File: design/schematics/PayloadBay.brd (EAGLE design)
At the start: 101.6 x 53.3 mm, 72 parts, among them IC1 MC33269ST-5.0T3, IC2 MC33269D-5.0, IC3 ATMEGA2560-16AU, IC4 ATMEGA8U2-MU, IC5 LM358D, IC6 LP2985-33DBVR, Q1 16MHz, Q2 16MHz, T2 FDN340P, X1 DC21MMX, Y1 16MHz, Y2 16MHz

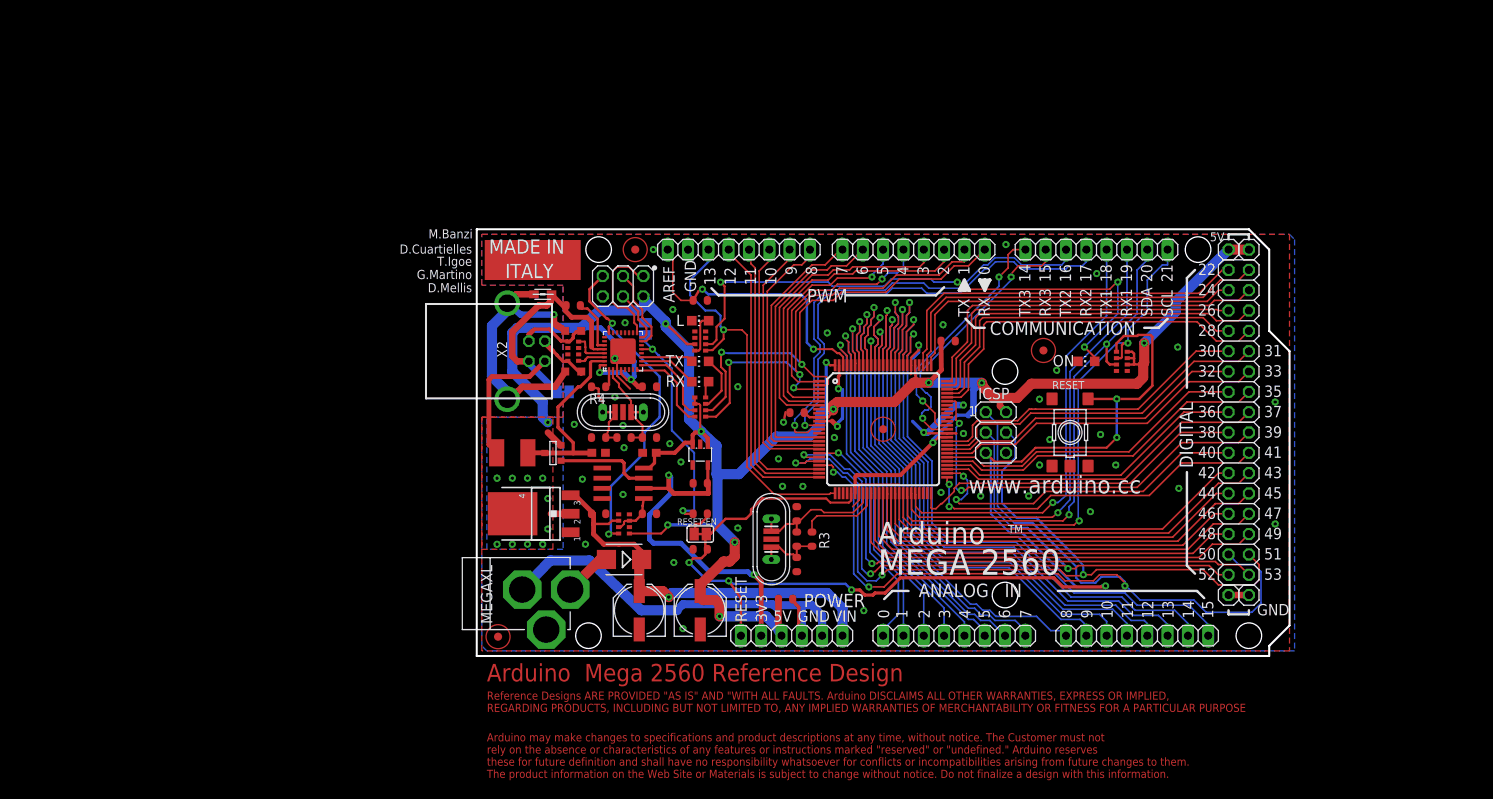
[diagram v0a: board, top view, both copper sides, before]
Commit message: updated schematics and board
* also added backup files made by eagle to gitignore
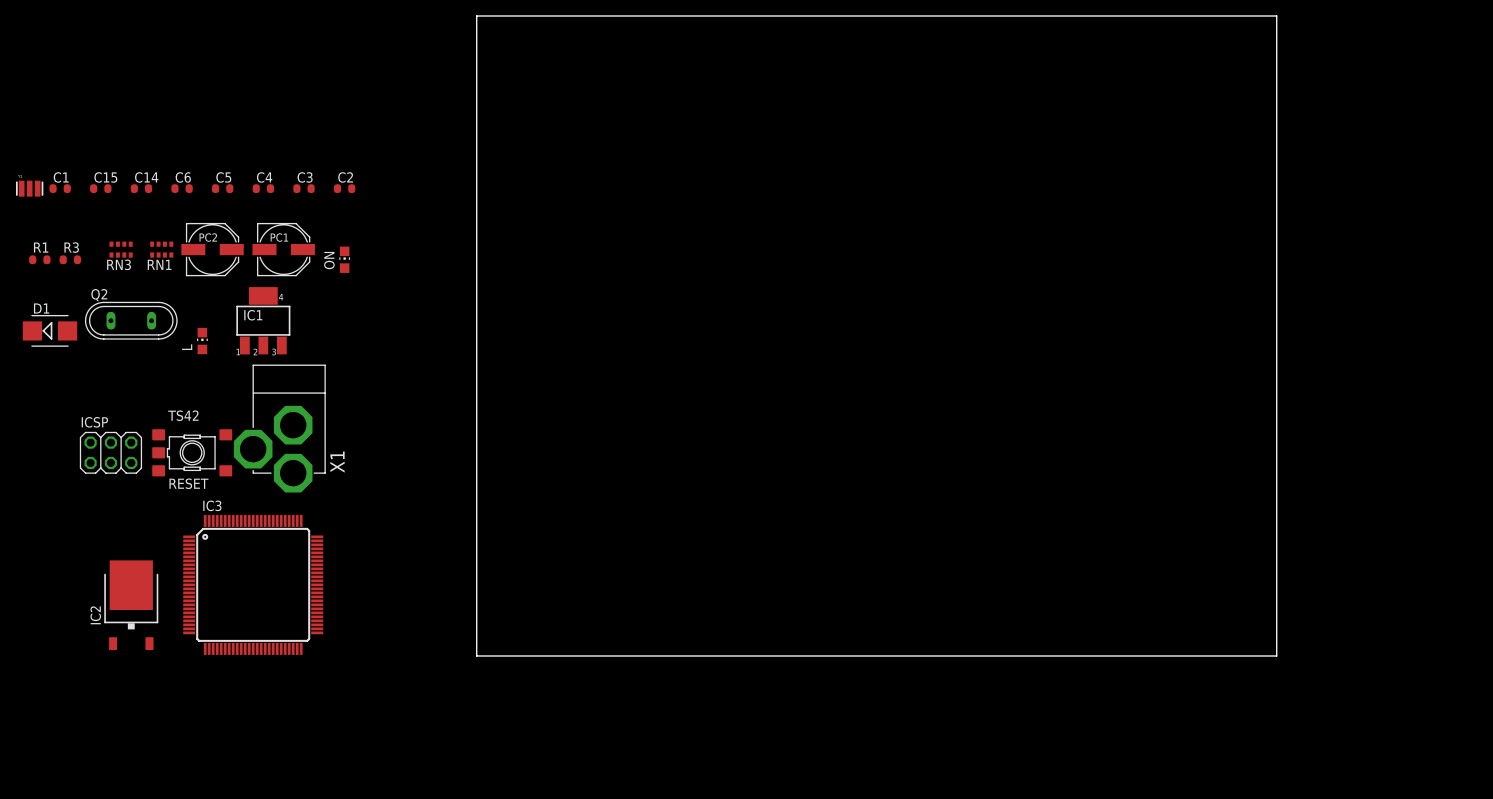
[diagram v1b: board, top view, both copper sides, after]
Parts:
- removed ADCH, ADCL, COMMUNICATION, PWMH, PWML: (no value), pinhead:1X08
- removed C10: 1u, SmartPrj:C0603-ROUND
- removed C11, C8: 100n, rcl:C0603
- removed C12, C13, C7, C9: 100n, SmartPrj:C0603-ROUND
- removed C16, C17: 22p, SmartPrj:C0603-ROUND
- removed F1: 500mA, rcl:L1812
- removed GROUND, RESET-EN, UBOOT: (no value), jumper:SJ
- removed IC4: ATMEGA8U2-MU, atmel:QFN32
- removed IC5: LM358D, linear:SO08
- removed IC6: LP2985-33DBVR, texas:SOT23-DBV
- removed ICSP1: ICSP, pinhead:2X03
- removed JP1, JP2, JP3, JP4: (no value), pinhead:1X01
- removed L1: BLM21, wuerth-elektronik:0805
- removed POWER: (no value), pinhead:1X06
- removed Q1: 16MHz, special:QS
- removed R2: 1M, SmartPrj:R0603-ROUND
- removed R4: 27R, SmartPrj:R0603-ROUND
- removed RN2: 22R, resistor-dil:CAY16
- removed RN4: 1k, resistor-dil:CAY16
- removed RN5: 10K, resistor-dil:CAT16
- removed RX, TX: YELLOW, led:CHIP-LED0805
- removed T2: FDN340P, zetex:SOT-23
- removed U$2, U$3, U$4, U$5: FIDUCIALMOUNT, SmartPrj:FIDUCIA-MOUNT
- removed X2: (no value), SmartPrj:PN61729
- removed XIOH, XIOL: (no value), pinhead:2X08
- removed Y2: 16MHz, SmartPrj:RESONATOR
- removed Z1, Z2: PGB1010604, varistor:CT/CN0603
- moved RN1 120.8 mm to (-39.4, 50.8), turned to 0 degrees
- moved ICSP 110.6 mm to (-45.7, 25.4), turned to 0 degrees
- moved RESET 109.8 mm to (-35.6, 25.4), turned to 0 degrees
- moved Y1 102.5 mm to (-55.9, 58.4), turned to 0 degrees
- moved R1 100.9 mm to (-54.6, 49.5), turned to 0 degrees
- moved R3 99.1 mm to (-50.8, 49.5), turned to 0 degrees
- moved C15 96.0 mm to (-47.0, 58.4), turned to 0 degrees
- moved C14 94.4 mm to (-41.9, 58.4), turned to 0 degrees
- moved ON 93.6 mm to (-16.5, 49.5), turned to 0 degrees
- moved C5 92.7 mm to (-31.8, 58.4)
- moved C1 91.8 mm to (-52.1, 58.4), turned to 0 degrees
- moved Q2 84.5 mm to (-43.2, 41.9), turned to 0 degrees
- moved C4 83.0 mm to (-26.7, 58.4)
- moved C6 81.8 mm to (-36.8, 58.4), turned to 0 degrees
- moved IC3 81.1 mm to (-27.9, 8.89)
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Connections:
- removed net +3V3: C13.2, IC5.6, IC6.5, POWER.2
- removed net CMP: C12.2, IC5.5, RN5.3, RN5.7
- removed net D+: RN2.5, X2.3, Z2.2
- removed net D-: RN2.8, X2.2, Z1.2
- removed net DTR: C7.1, IC4.13, UBOOT.1
- removed net GATE_CMD: IC5.7, T2.3
- removed net M8RXD: IC4.9, RN4.7
- removed net M8TXD: IC4.8, RN4.8
- removed net MISO2: IC4.17, ICSP1.1
- removed net MOSI2: IC4.16, ICSP1.4
- removed net N$54: RN4.4, RX.A
- removed net N$55: RN4.3, TX.A
- removed net RD+: IC4.29, RN2.4
- removed net RD-: IC4.30, RN2.1
- removed net RESET2: IC4.24, ICSP1.5, RN5.8
- removed net RXL: IC4.10, RX.C
- removed net SCK2: IC4.15, ICSP1.3
- removed net TXL: IC4.11, TX.C
- removed net UGND: C10.2, GROUND.1, IC4.28, L1.1, X2.4
- removed net USBVCC: C8.1, F1.1, IC4.31, T2.1
- removed net USHIELD: L1.2, X2.P$1, X2.P$2, Z1.1, Z2.1
- removed net VUCAP: C10.1, IC4.27
- removed net XT1: C16.1, Q1.2, R2.1, R4.2, Y2.3
- removed net XT1R: IC4.1, R4.1
- removed net XT2: C17.1, IC4.2, Q1.1, R2.2, Y2.1
- removed net XVCC: F1.2, X2.1
- net +5V: no longer C11.2, C9.1, IC4.32, IC4.4, IC5.8, IC6.1, IC6.3, ICSP1.2, JP1.1, JP2.1, POWER.3, RN4.5, RN4.6, RN5.1, T2.2
- net ADC0: no longer ADCL.1
- net ADC1: no longer ADCL.2
- net ADC10: no longer ADCH.3
- net ADC11: no longer ADCH.4
- net ADC12: no longer ADCH.5
- net ADC13: no longer ADCH.6
- net ADC14: no longer ADCH.7
- net ADC15: no longer ADCH.8
- net ADC2: no longer ADCL.3
- net ADC3: no longer ADCL.4
- net ADC4: no longer ADCL.5
- net ADC5: no longer ADCL.6
- net ADC6: no longer ADCL.7
- net ADC7: no longer ADCL.8
- net ADC8: no longer ADCH.1
- net ADC9: no longer ADCH.2
- net AREF: no longer PWMH.8
- net GND: no longer C11.1, C12.1, C13.1, C16.2, C17.2, C8.2, C9.2, GROUND.2, IC4.3, IC4.EXP, IC5.2, IC5.3, IC5.4, IC6.2, ICSP1.6, JP3.1, JP4.1, POWER.4, POWER.5, PWMH.7, RN5.2, UBOOT.2, Y2.2
- net PA0: no longer XIOH.16
- net PA1: no longer XIOH.15
- net PA2: no longer XIOH.14
- net PA3: no longer XIOH.13
- net PA4: no longer XIOH.12
- net PA5: no longer XIOH.11
- net PA6: no longer XIOH.10
- net PA7: no longer XIOH.9
- net PB0: no longer XIOL.1
- net PB1: no longer XIOL.2
- net PB2: no longer XIOL.3
- net PB3: no longer XIOL.4
- net PB4: no longer PWMH.3
- net PB5: no longer PWMH.4
- net PB6: no longer PWMH.5
- net PB7: no longer PWMH.6
- net PC0: no longer XIOH.1
- net PC1: no longer XIOH.2
- net PC2: no longer XIOH.3
- net PC3: no longer XIOH.4
- net PC4: no longer XIOH.5
- net PC5: no longer XIOH.6
- net PC6: no longer XIOH.7
- net PC7: no longer XIOH.8
- net PD7: no longer XIOL.16
- net PE0: no longer PWML.1, RN4.2
- net PE1: no longer PWML.2, RN4.1
- net PE3: no longer PWML.6
- net PE4: no longer PWML.3
- net PE5: no longer PWML.4
- net PG0: no longer XIOL.13
- net PG1: no longer XIOL.14
- net PG2: no longer XIOL.15
- net PG5: no longer PWML.5
- net PH3: no longer PWML.7
- net PH4: no longer PWML.8
- net PH5: no longer PWMH.1
- net PH6: no longer PWMH.2
- net PL0: no longer XIOL.5
- net PL1: no longer XIOL.6
- net PL2: no longer XIOL.7
- net PL3: no longer XIOL.8
- net PL4: no longer XIOL.9
- net PL5: no longer XIOL.10
- net PL6: no longer XIOL.11
- net PL7: no longer XIOL.12
- net RESET: no longer C7.2, POWER.1, RESET-EN.1, RESET-EN.2
- net RXD1: no longer COMMUNICATION.3
- net RXD2: no longer COMMUNICATION.5
- net RXD3: no longer COMMUNICATION.7
- net SCL: no longer COMMUNICATION.1
- net SDA: no longer COMMUNICATION.2
- net TXD1: no longer COMMUNICATION.4
- net TXD2: no longer COMMUNICATION.6
- net TXD3: no longer COMMUNICATION.8
- net VIN: no longer POWER.6, RN5.6
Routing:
- net +5V: track 292.7 -> 0.00 mm, vias 24 -> 0
- net RESET: track 164.2 -> 0.00 mm, vias 6 -> 0
- net PB3: track 115.5 -> 0.00 mm, vias 3 -> 0
- net GND: track 105.1 -> 0.00 mm, vias 47 -> 0
- net PB2: track 104.6 -> 0.00 mm, vias 3 -> 0
- net PB1: track 91.3 -> 0.00 mm, vias 3 -> 0
- net ADC13: track 75.2 -> 0.00 mm, vias 1 -> 0
- net ADC14: track 72.8 -> 0.00 mm, vias 1 -> 0
- net N$3: track 72.7 -> 0.00 mm, vias 4 -> 0
- net ADC11: track 71.4 -> 0.00 mm, vias 1 -> 0
- net ADC12: track 71.3 -> 0.00 mm, vias 1 -> 0
- net ADC15: track 70.6 -> 0.00 mm, vias 1 -> 0
- net SCL: track 68.5 -> 0.00 mm, vias 2 -> 0
- net PB0: track 66.4 -> 0.00 mm, vias 2 -> 0
- net ADC10: track 64.9 -> 0.00 mm, vias 1 -> 0
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- removed copper zone on layer 1, net +5V
- removed copper zone on layer 16, net +5V
- removed copper zone on layer 1, net GND
- removed copper zone on layer 16, net GND
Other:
- board size 101.6 x 53.3 mm -> 100 x 80 mm
- board text removed: "0"
- board text removed: "1"
- board text removed: "10"
- board text removed: "11"
- board text removed: "12"
- board text removed: "13"
- board text removed: "14"
- board text removed: "15"
- board text removed: "16"
- board text removed: "17"
- board text removed: "18"
- board text removed: "19"
- board text removed: "2"
- board text removed: "20"
- board text removed: "21"
- board text removed: "22"
- board text removed: "24"
- board text removed: "26"
- board text removed: "28"
- board text removed: "3"
- board text removed: "30"
- board text removed: "31"
- board text removed: "32"
- board text removed: "33"
- board text removed: "34"
- board text removed: "35"
- board text removed: "36"
- board text removed: "37"
- board text removed: "38"
- board text removed: "39"
- board text removed: "3V3"
- board text removed: "4"
- board text removed: "40"
- board text removed: "41"
- board text removed: "42"
- board text removed: "43"
- board text removed: "44"
- board text removed: "45"
- board text removed: "46"
- board text removed: "47"
- board text removed: "48"
- board text removed: "49"
- board text removed: "5"
- board text removed: "50"
- board text removed: "51"
- board text removed: "52"
- board text removed: "53"
- board text removed: "5V"
- board text removed: "6"
- board text removed: "7"
- board text removed: "8"
- board text removed: "9"
- board text removed: "ANALOG IN"
- board text removed: "AREF"
- board text removed: "Arduino"
- board text removed: "Arduino Mega 2560 Reference Design"
- board text removed: "Arduino may make changes to specifications and product descriptions at any time, without notice. The Customer must not rely on the absence or characteristics of any features or instructions marked "reserved" or "undefined." Arduino reserves these for future definition and shall have no responsibility whatsoever for conflicts or incompatibilities arising from future changes to them. The product in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"
- board text removed: "D.Cuartielles"
- board text removed: "D.Mellis"
- board text removed: "DIGITAL"
- board text removed: "G.Martino"
- board text removed: "GND"
- board text removed: "ITALY"
- board text removed: "L"
- board text removed: "M.Banzi"
- board text removed: "MADE IN"
- board text removed: "MEGA 2560"
- board text removed: "MEGAXL"
- board text removed: "PC1"
- board text removed: "PC2"
- board text removed: "PWM"
- board text removed: "RESET"
- board text removed: "RX"
- board text removed: "RX1"
- board text removed: "RX2"
- board text removed: "RX3"
- board text removed: "Reference Designs ARE PROVIDED "AS IS" AND "WITH ALL FAULTS. Arduino DISCLAIMS ALL OTHER WARRANTIES, EXPRESS OR IMPLIED, REGARDING PRODUCTS, INCLUDING BUT NOT LIMITED TO, ANY IMPLIED WARRANTIES OF MERCHANTABILITY OR FITNESS FOR A PARTICULAR PURPOSE"
- board text removed: "SCL"
- board text removed: "SDA"
- board text removed: "T.Igoe"
- board text removed: "TM"
- board text removed: "TX"
- board text removed: "TX1"
- board text removed: "TX2"
- board text removed: "TX3"
- board text removed: "VIN"
- board text removed: "designed by"
- board text removed: "tinker it"
- board text removed: "www.arduino.cc"
